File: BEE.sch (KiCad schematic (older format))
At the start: 30 parts, among them J1 RPI1_header, J10 Conn_01x02, J11 Conn_01x02, J12 Conn_01x02, J2 BEE_header, J3 Conn_01x03, J4 Conn_01x06, J5 Conn_01x03, J6 Conn_01x05, J7 Conn_01x03, J8 Conn_01x08, J9 Conn_01x02, SW1 SW_Push, SW2 SW_Push, SW3 SW_Push, U1 MCP3008, U2 MCP4911

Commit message: no signal reorder
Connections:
- net labels removed: GNDA
- wire segments 172 -> 171

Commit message: wip:pcb routed, raspi header can be moved right
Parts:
- removed J2: BEE_header, Connector_PinHeader_2.54mm:PinHeader_1x28_P2.54mm_Vertical, symbol BEE:BEE_header
- removed J3, J5: Conn_01x03, Connector_PinHeader_2.54mm:PinHeader_1x03_P2.54mm_Vertical, symbol Connector_Generic:Conn_01x03
- removed J6: Conn_01x05, Connector_PinHeader_2.54mm:PinHeader_1x05_P2.54mm_Vertical, symbol Connector_Generic:Conn_01x05
- added J15: Conn_01x09, Connector_PinHeader_2.54mm:PinHeader_1x09_P2.54mm_Vertical, symbol Connector_Generic:Conn_01x09
- added J2: Conn_02x05_Odd_Even, Connector_PinHeader_2.54mm:PinHeader_2x05_P2.54mm_Vertical, symbol Connector_Generic:Conn_02x05_Odd_Even
- added J3: Conn_02x03_Odd_Even, Connector_PinHeader_2.54mm:PinHeader_2x03_P2.54mm_Vertical, symbol Connector_Generic:Conn_02x03_Odd_Even
- added J5: Conn_02x10_Odd_Even, Connector_PinHeader_2.54mm:PinHeader_2x10_P2.54mm_Vertical, symbol Connector_Generic:Conn_02x10_Odd_Even
- added J6: Conn_01x08, Connector_PinHeader_2.54mm:PinHeader_1x08_P2.54mm_Vertical, symbol Connector_Generic:Conn_01x08
- added R7: 0, Resistor_SMD:R_0805_2012Metric_Pad1.15x1.40mm_HandSolder, symbol Device:R
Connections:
- net labels added: BCM12_PWM0, BCM13_PWM1, BCM18_PWM0, BCM23_RTCK
- net labels removed: BCM12, BCM13, BCM18_PWM, BCM23
- wire segments 171 -> 193
- no-connect marks 0 -> 3
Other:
- note added: "JTAG connector:\nUsing pins compatible with old raspberry pi's\n\nBCM22 TRST ALT4\nBCM4 TDI ALT5\nBCM27 TMS ALT4\nBCM25 TCLK ALT4\nBCM23 RTCK ALT4\nBCM24 TDO ALT4"
- moved on the sheet: BZ1, C2, C3, J10, J12, J7, J9, U2

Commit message: wip some traces re-routed
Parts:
- J10, J11, J12, J9: footprint Connector_PinSocket_2.54mm:PinSocket_1x02_P2.54mm_Vertical -> Connector_PinHeader_2.54mm:PinHeader_1x02_P2.54mm_Vertical
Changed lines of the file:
@@
 F 0 "J9" H 7450 4550 50  0000 C CNN
 F 1 "Conn_01x02" H 7400 4950 50  0000 C CNN
-F 2 "Connector_PinSocket_2.54mm:PinSocket_1x02_P2.54mm_Vertical" H 7450 4750 50  0001 C CNN
+F 2 "Connector_PinHeader_2.54mm:PinHeader_1x02_P2.54mm_Vertical" H 7450 4750 50  0001 C CNN
 F 3 "https://www.mouser.es/datasheet/2/418/NG_CD_640456_W3-1255681.pdf" H 7450 4750 50  0001 C CNN
 F 4 "Mouser" H -100 850 50  0001 C CNN "Distributor"
@@
 F 0 "J11" V 10050 1700 50  0000 C CNN
 F 1 "Conn_01x02" V 10150 1550 50  0000 C CNN
-F 2 "Connector_PinSocket_2.54mm:PinSocket_1x02_P2.54mm_Vertical" H 10050 1550 50  0001 C CNN
+F 2 "Connector_PinHeader_2.54mm:PinHeader_1x02_P2.54mm_Vertical" H 10050 1550 50  0001 C CNN
 F 3 "https://www.mouser.es/datasheet/2/418/NG_CD_640456_W3-1255681.pdf" H 10050 1550 50  0001 C CNN
 F 4 "Mouser" H 2500 -2350 50  0001 C CNN "Distributor"
@@
 F 0 "J10" H 9600 4450 50  0000 C CNN
 F 1 "Conn_01x02" V 9700 4350 50  0000 C CNN
-F 2 "Connector_PinSocket_2.54mm:PinSocket_1x02_P2.54mm_Vertical" H 9600 4350 50  0001 C CNN
+F 2 "Connector_PinHeader_2.54mm:PinHeader_1x02_P2.54mm_Vertical" H 9600 4350 50  0001 C CNN
 F 3 "https://www.mouser.es/datasheet/2/418/NG_CD_640456_W3-1255681.pdf" H 9600 4350 50  0001 C CNN
 F 4 "Mouser" H 2050 450 50  0001 C CNN "Distributor"
@@
 F 0 "J12" H 10050 4750 50  0000 C CNN
 F 1 "Conn_01x02" V 10150 4650 50  0000 C CNN
-F 2 "Connector_PinSocket_2.54mm:PinSocket_1x02_P2.54mm_Vertical" H 10050 4650 50  0001 C CNN
+F 2 "Connector_PinHeader_2.54mm:PinHeader_1x02_P2.54mm_Vertical" H 10050 4650 50  0001 C CNN
 F 3 "https://www.mouser.es/datasheet/2/418/NG_CD_640456_W3-1255681.pdf" H 10050 4650 50  0001 C CNN
 F 4 "Mouser" H 2500 750 50  0001 C CNN "Distributor"

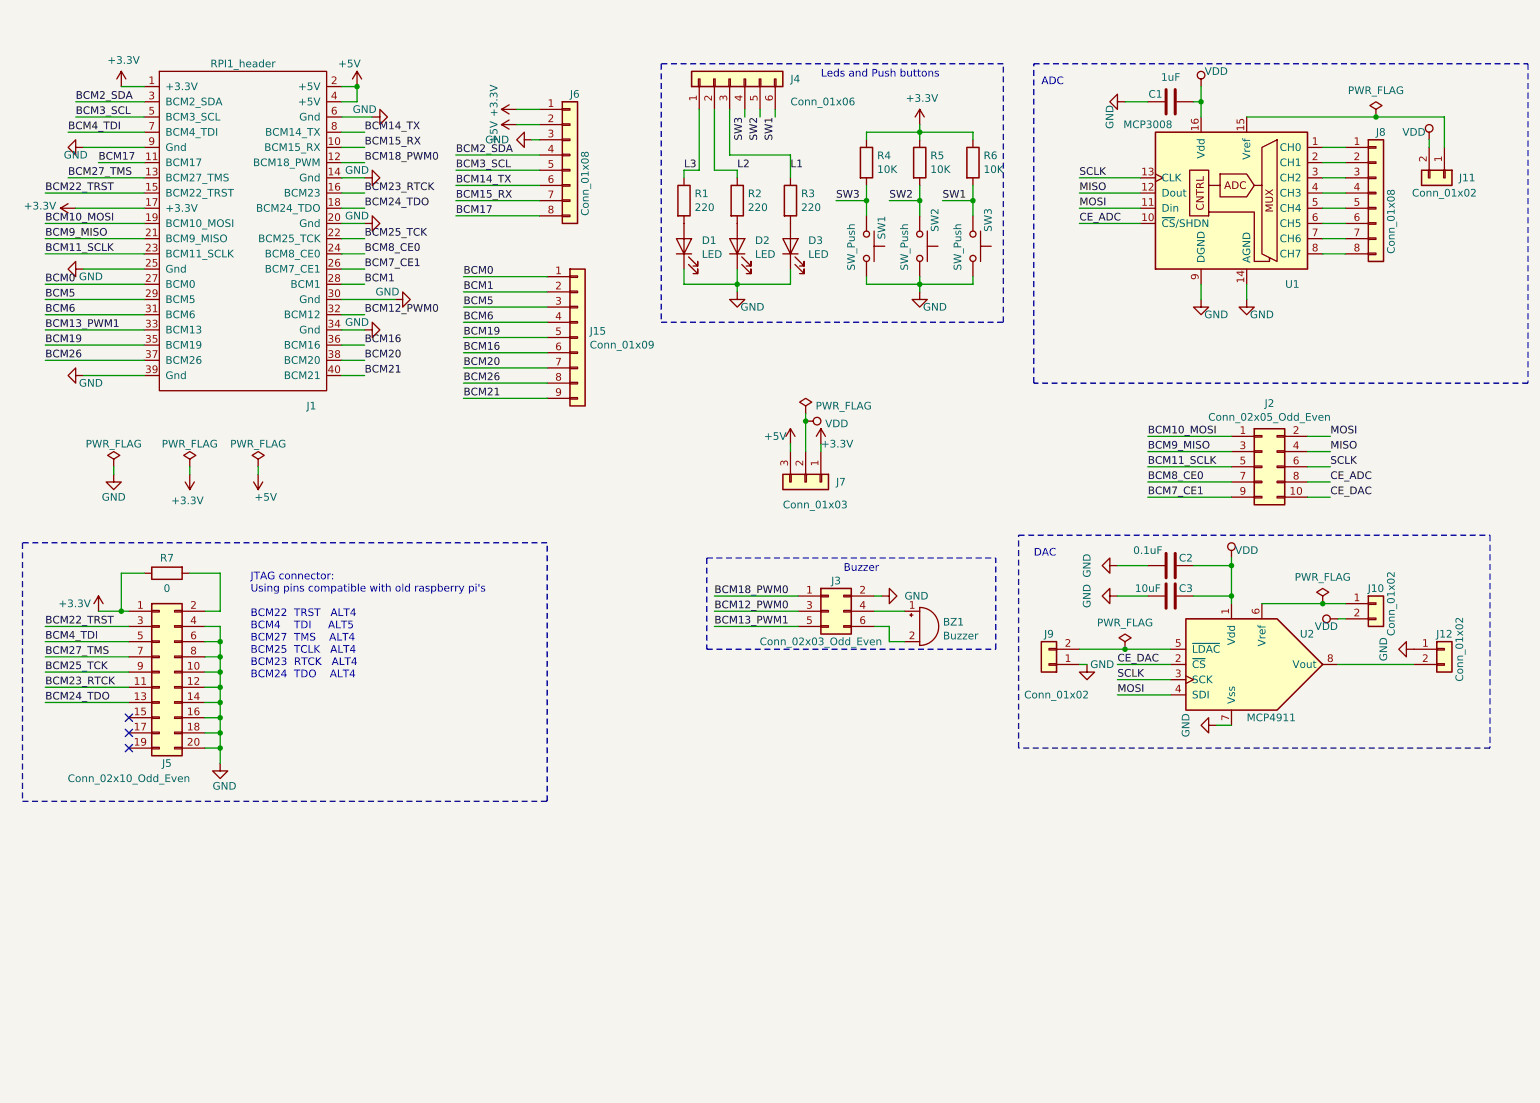
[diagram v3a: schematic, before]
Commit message: wip: with mounting holes, board a little bit bigger
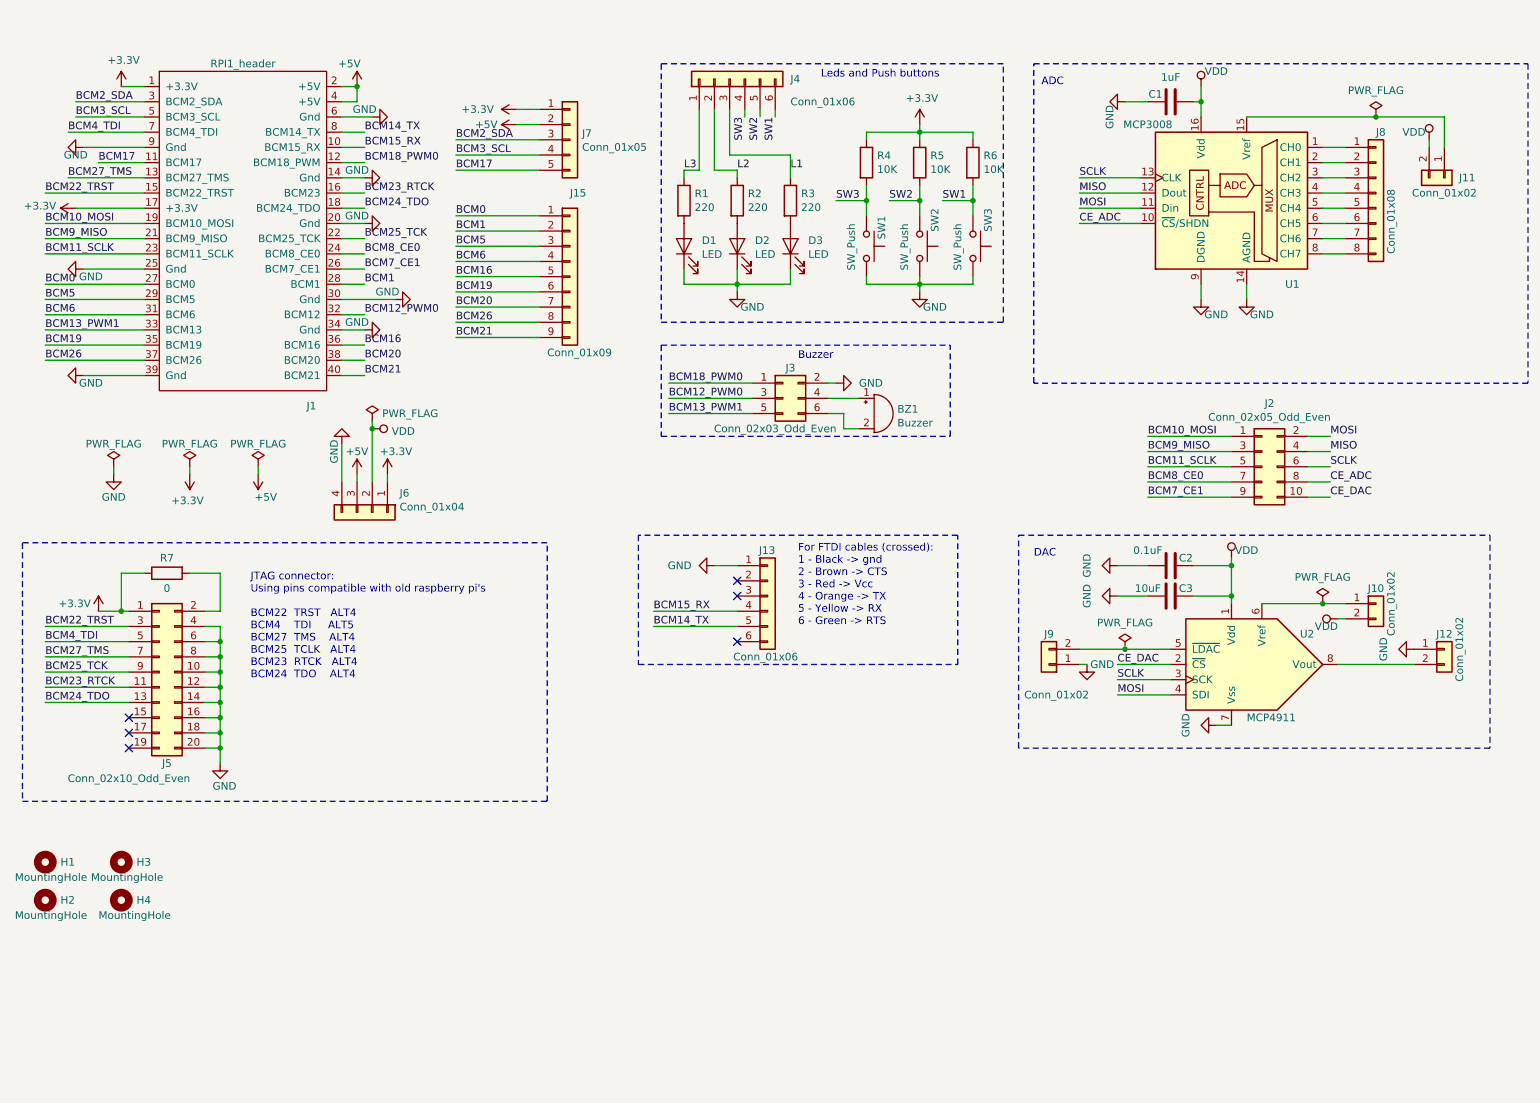
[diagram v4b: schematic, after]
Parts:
- removed J6: Conn_01x08, Connector_PinHeader_2.54mm:PinHeader_1x08_P2.54mm_Vertical, symbol Connector_Generic:Conn_01x08
- removed J7: Conn_01x03, Connector_PinHeader_2.54mm:PinHeader_1x03_P2.54mm_Vertical, symbol Connector_Generic:Conn_01x03
- added H1, H2, H3, H4: MountingHole, MountingHole:MountingHole_2.5mm, symbol Mechanical:MountingHole
- added J13: Conn_01x06, Connector_PinHeader_2.54mm:PinHeader_1x06_P2.54mm_Vertical, symbol Connector_Generic:Conn_01x06
- added J6: Conn_01x04, Connector_PinHeader_2.54mm:PinHeader_1x04_P2.54mm_Vertical, symbol Connector_Generic:Conn_01x04
- added J7: Conn_01x05, Connector_PinHeader_2.54mm:PinHeader_1x05_P2.54mm_Vertical, symbol Connector_Generic:Conn_01x05
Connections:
- net +3V3: now also J6.1 (Pin_1), J7.1 (Pin_1)
- net +5V: now also J6.3 (Pin_3), J7.2 (Pin_2)
- net BCM14_TX: now also J13.5 (Pin_5)
- net BCM15_RX: now also J13.4 (Pin_4)
- net BCM16: now also J15.5 (Pin_5); no longer J15.6 (Pin_6)
- net BCM17: now also J7.5 (Pin_5)
- net BCM19: now also J15.6 (Pin_6); no longer J15.5 (Pin_5)
- net BCM2_SDA: now also J7.3 (Pin_3)
- net BCM3_SCL: now also J7.4 (Pin_4)
- net GND: now also J13.1 (Pin_1), J6.4 (Pin_4)
- net VDD: now also J6.2 (Pin_2)
- no-connect marks 3 -> 6
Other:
- note added: "For FTDI cables (crossed):\n1 - Black -> gnd\n2 - Brown -> CTS\n3 - Red -> Vcc\n4 - Orange -> TX\n5 - Yellow -> RX\n6 - Green -> RTS"
- moved on the sheet: BZ1, J15, J3

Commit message: uart connector with jumpers to select crossed or direct connection. rerouted and labeled
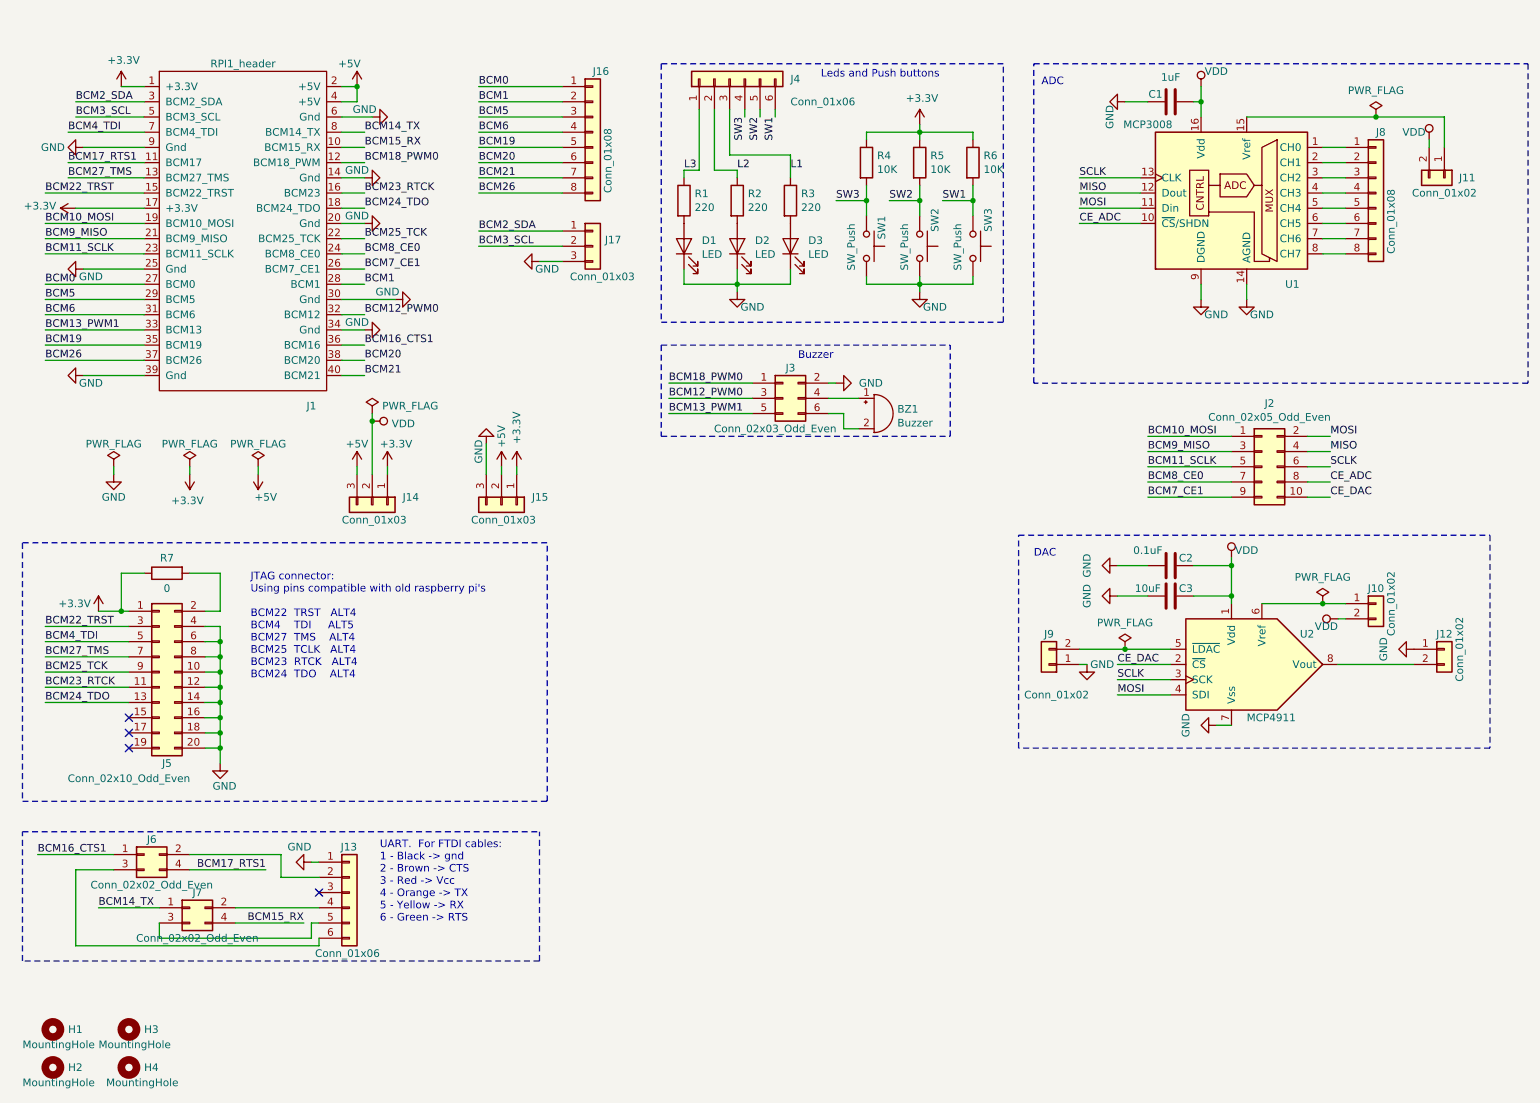
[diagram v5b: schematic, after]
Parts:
- removed J15: Conn_01x09, Connector_PinHeader_2.54mm:PinHeader_1x09_P2.54mm_Vertical, symbol Connector_Generic:Conn_01x09
- removed J6: Conn_01x04, Connector_PinHeader_2.54mm:PinHeader_1x04_P2.54mm_Vertical, symbol Connector_Generic:Conn_01x04
- removed J7: Conn_01x05, Connector_PinHeader_2.54mm:PinHeader_1x05_P2.54mm_Vertical, symbol Connector_Generic:Conn_01x05
- added J14, J15, J17: Conn_01x03, Connector_PinHeader_2.54mm:PinHeader_1x03_P2.54mm_Vertical, symbol Connector_Generic:Conn_01x03
- added J16: Conn_01x08, Connector_PinHeader_2.54mm:PinHeader_1x08_P2.54mm_Vertical, symbol Connector_Generic:Conn_01x08
- added J6, J7: Conn_02x02_Odd_Even, Connector_PinHeader_2.54mm:PinHeader_2x02_P2.54mm_Vertical, symbol Connector_Generic:Conn_02x02_Odd_Even
- J5: Distributor Moser -> Mouser
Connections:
- net +3V3: now also J14.1 (Pin_1), J15.1 (Pin_1)
- net +5V: now also J14.3 (Pin_3), J15.2 (Pin_2)
- net BCM0: now also J16.1 (Pin_1)
- net BCM1: now also J16.2 (Pin_2)
- net BCM14_TX: now also J7.1 (Pin_1); no longer J13.5 (Pin_5)
- net BCM15_RX: now also J7.4 (Pin_4); no longer J13.4 (Pin_4)
- net BCM19: now also J16.5 (Pin_5)
- net BCM20: now also J16.6 (Pin_6)
- net BCM21: now also J16.7 (Pin_7)
- net BCM26: now also J16.8 (Pin_8)
- net BCM2_SDA: now also J17.1 (Pin_1)
- net BCM3_SCL: now also J17.2 (Pin_2)
- net BCM5: now also J16.3 (Pin_3)
- net BCM6: now also J16.4 (Pin_4)
- net GND: now also J15.3 (Pin_3), J17.3 (Pin_3)
- net VDD: now also J14.2 (Pin_2)
- net at J13.2 (Pin_2): now also J6.2 (Pin_2)
- net at J13.6 (Pin_6): now also J6.3 (Pin_3)
- net BCM16 renamed BCM16_CTS1
- net BCM16_CTS1: now also J6.1 (Pin_1)
- net BCM17 renamed BCM17_RTS1
- net BCM17_RTS1: now also J6.4 (Pin_4)
- new net: J13.4 (Pin_4), J7.2 (Pin_2)
- new net: J13.5 (Pin_5), J7.3 (Pin_3)
- no-connect marks 6 -> 4
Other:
- note added: "UART. For FTDI cables:\n1 - Black -> gnd\n2 - Brown -> CTS\n3 - Red -> Vcc\n4 - Orange -> TX\n5 - Yellow -> RX\n6 - Green -> RTS"
- note removed: "For FTDI cables (crossed):\n1 - Black -> gnd\n2 - Brown -> CTS\n3 - Red -> Vcc\n4 - Orange -> TX\n5 - Yellow -> RX\n6 - Green -> RTS"
- moved on the sheet: H1, H2, H3, H4, J13
